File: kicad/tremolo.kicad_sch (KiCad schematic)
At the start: 17 parts, among them IC2 TL072CP

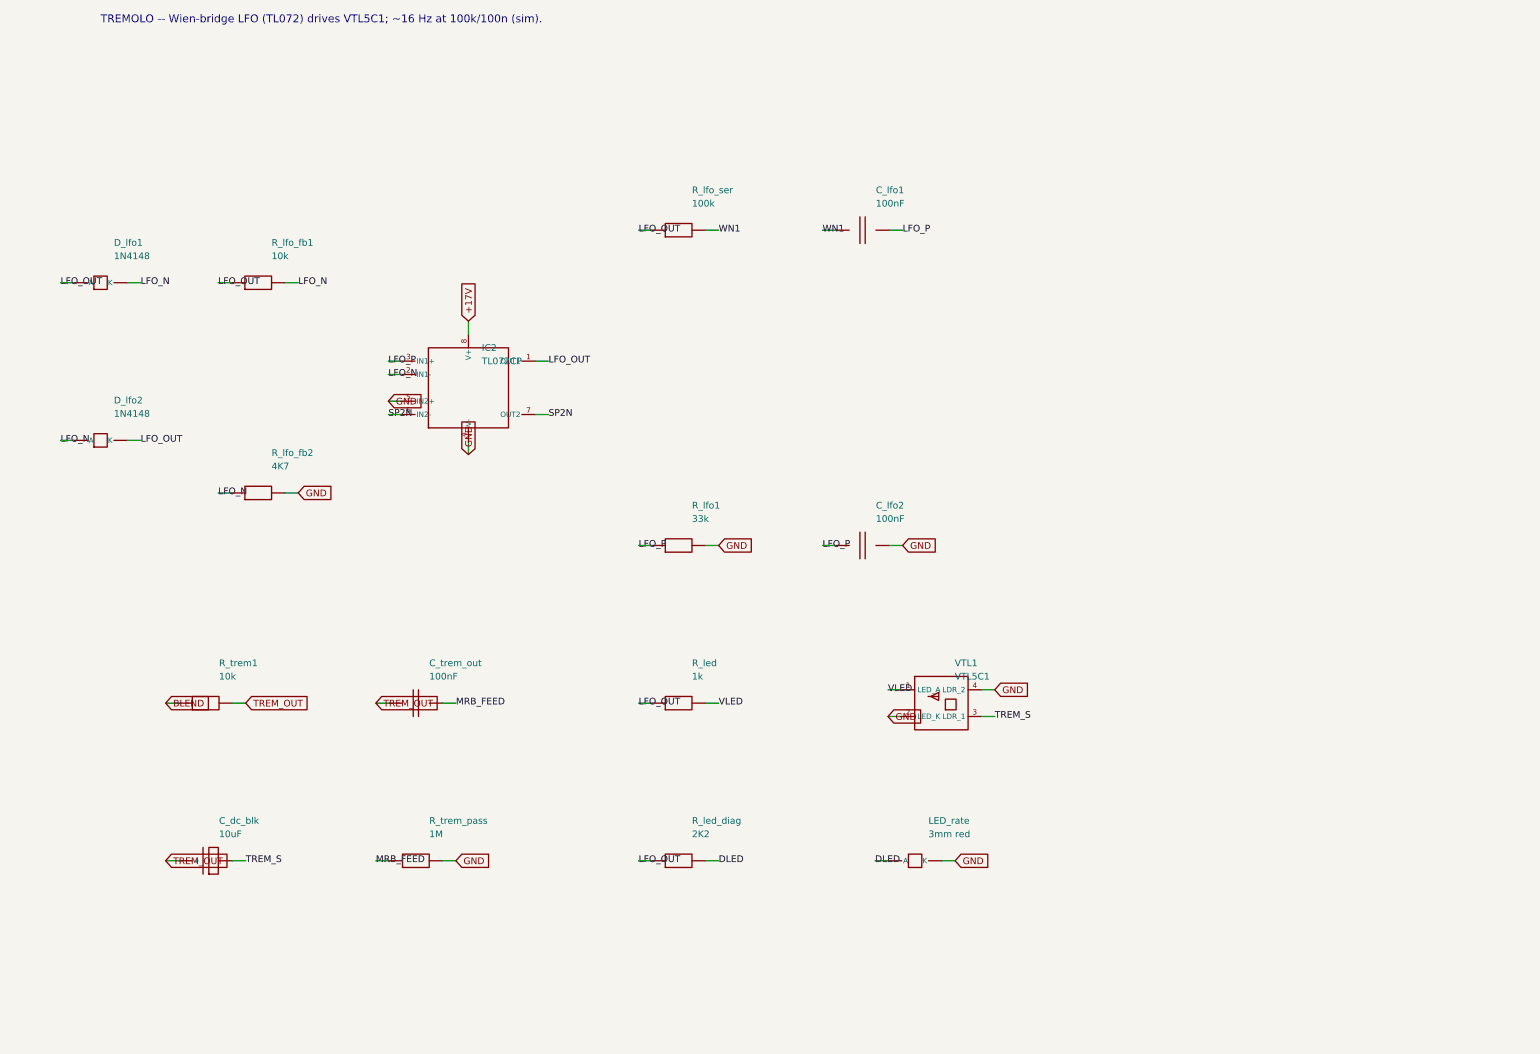
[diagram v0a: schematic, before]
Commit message: Schematic passes KiCad 8 ERC (0 violations); add op-amp mid-rail bias
Installed KiCad 8.0.9 and ran a real Electrical Rules Check on the generated
hierarchy. Drove it to 0 violations:
- snapped every pin/wire endpoint to the 1.27 mm connection grid (was 338
  endpoint_off_grid violations)
- gave the footswitch lines FS_REV/FS_TREM/FS_MRB a real second endpoint via
  100k control pulldowns on the reverb/tremolo/mrb sheets (was 3 dangling labels)

Also made the single-supply TL072 stages electrically real: added a mid-rail
VBIAS network (R_vb1/R_vb2 + C_vb on the Power Supply sheet) and referenced the
reverb driver and tremolo LFO inputs/gain-returns to VBIAS instead of GND
(design addition, flagged in the sheet notes).

Result: kicad-cli 8.0.9 sch erc -> 0 violations; netlist 102 components, 58
nets, 0 unconnected pins; VBIAS spans 10 nodes. Updated SCHEMATIC-BUILD.md,
kicad/README.md, CHANGELOG.md.

https://claude.ai/code/session_01PkrfUi9tvZfLvudJ7h23qD
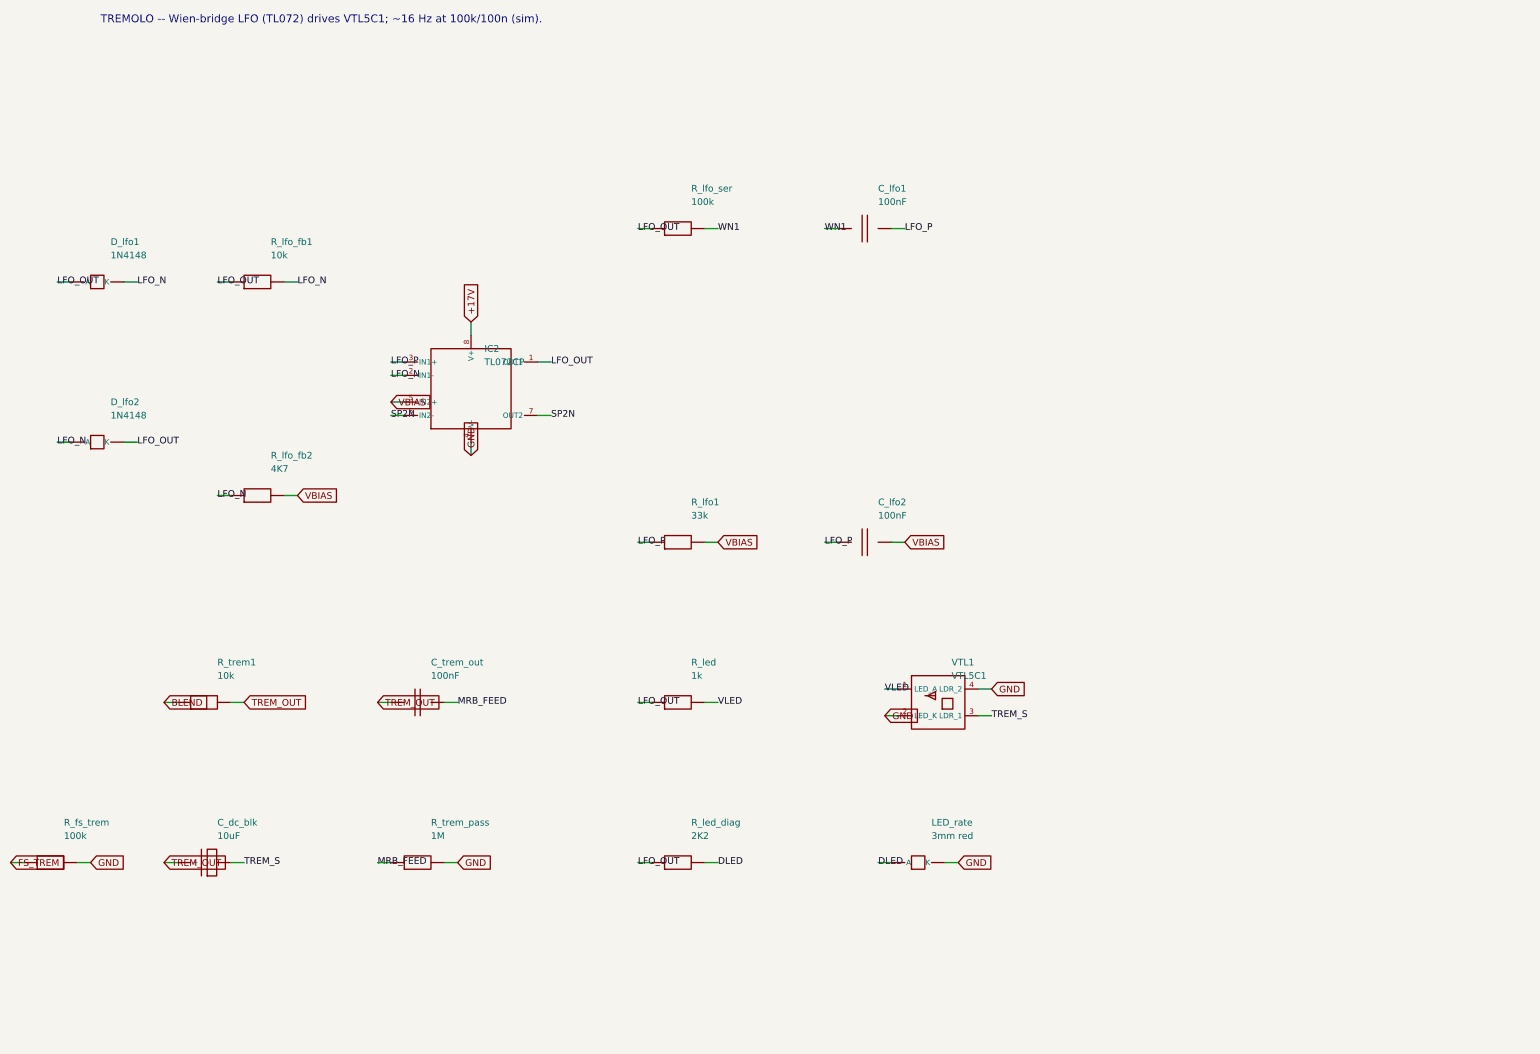
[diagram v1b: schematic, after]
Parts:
- added R_fs_trem: 100k, symbol cr_primitives:R
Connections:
- net GND: now also R_fs_trem.2; no longer C_lfo2.2, IC2.5 (IN2+), R_lfo1.2, R_lfo_fb2.2
- new net FS_TREM: R_fs_trem.1
- new net VBIAS: C_lfo2.2, IC2.5 (IN2+), R_lfo1.2, R_lfo_fb2.2

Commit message: Generate auto-placed PCB (102 footprints, GND pour, board outline)
Build cambridge_reverb.kicad_pcb from the schematic via kicad/gen/gen_pcb.py
(KiCad 8 pcbnew API): assign a THT footprint to every component (standard libs
for generics + the project footprints for VTL5C1 and the 1H toroid), place all
102 footprints (off-board connectors on a bottom wiring-edge strip, toroid in a
reserved spot), assign all 58 nets to pads, draw a 190x115 mm Edge.Cuts outline,
and pour a bottom-layer GND plane. Footprint assignments also carry into the
schematic symbols.

The board opens in KiCad and the ratsnest matches the ERC-clean schematic. It is
placed but NOT routed: kicad-cli pcb drc is dominated by 130 unconnected
(unrouted signal nets; GND is poured) plus cosmetic silk/courtyard overlaps from
dense auto-placement at chassis size -- documented in kicad/PCB-NOTES.md with the
remaining hand-work (placement into floor-plan zones, routing, DRC-to-zero,
Gerbers). Net classes (Default/Power/HighCurrent) carry over for routing.

Also: schematic resistor footprint switched to the compact vertical variant;
gitignore DRC/ERC .rpt reports.

https://claude.ai/code/session_01PkrfUi9tvZfLvudJ7h23qD
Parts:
- C_dc_blk: footprint (none) -> Capacitor_THT:CP_Radial_D8.0mm_P3.50mm
- C_lfo1, C_lfo2, C_trem_out: footprint (none) -> Capacitor_THT:C_Disc_D7.5mm_W2.5mm_P5.00mm
- D_lfo1, D_lfo2: footprint (none) -> Diode_THT:D_DO-41_SOD81_P10.16mm_Horizontal
- IC2: footprint (none) -> Package_DIP:DIP-8_W7.62mm
- LED_rate: footprint (none) -> LED_THT:LED_D3.0mm
- R_fs_trem, R_led, R_led_diag, R_lfo1, R_lfo_fb1, R_lfo_fb2, R_lfo_ser, R_trem1, R_trem_pass: footprint (none) -> Resistor_THT:R_Axial_DIN0207_L6.3mm_D2.5mm_P5.08mm_Vertical
- VTL1: footprint (none) -> cambridge_reverb:VTL5C1

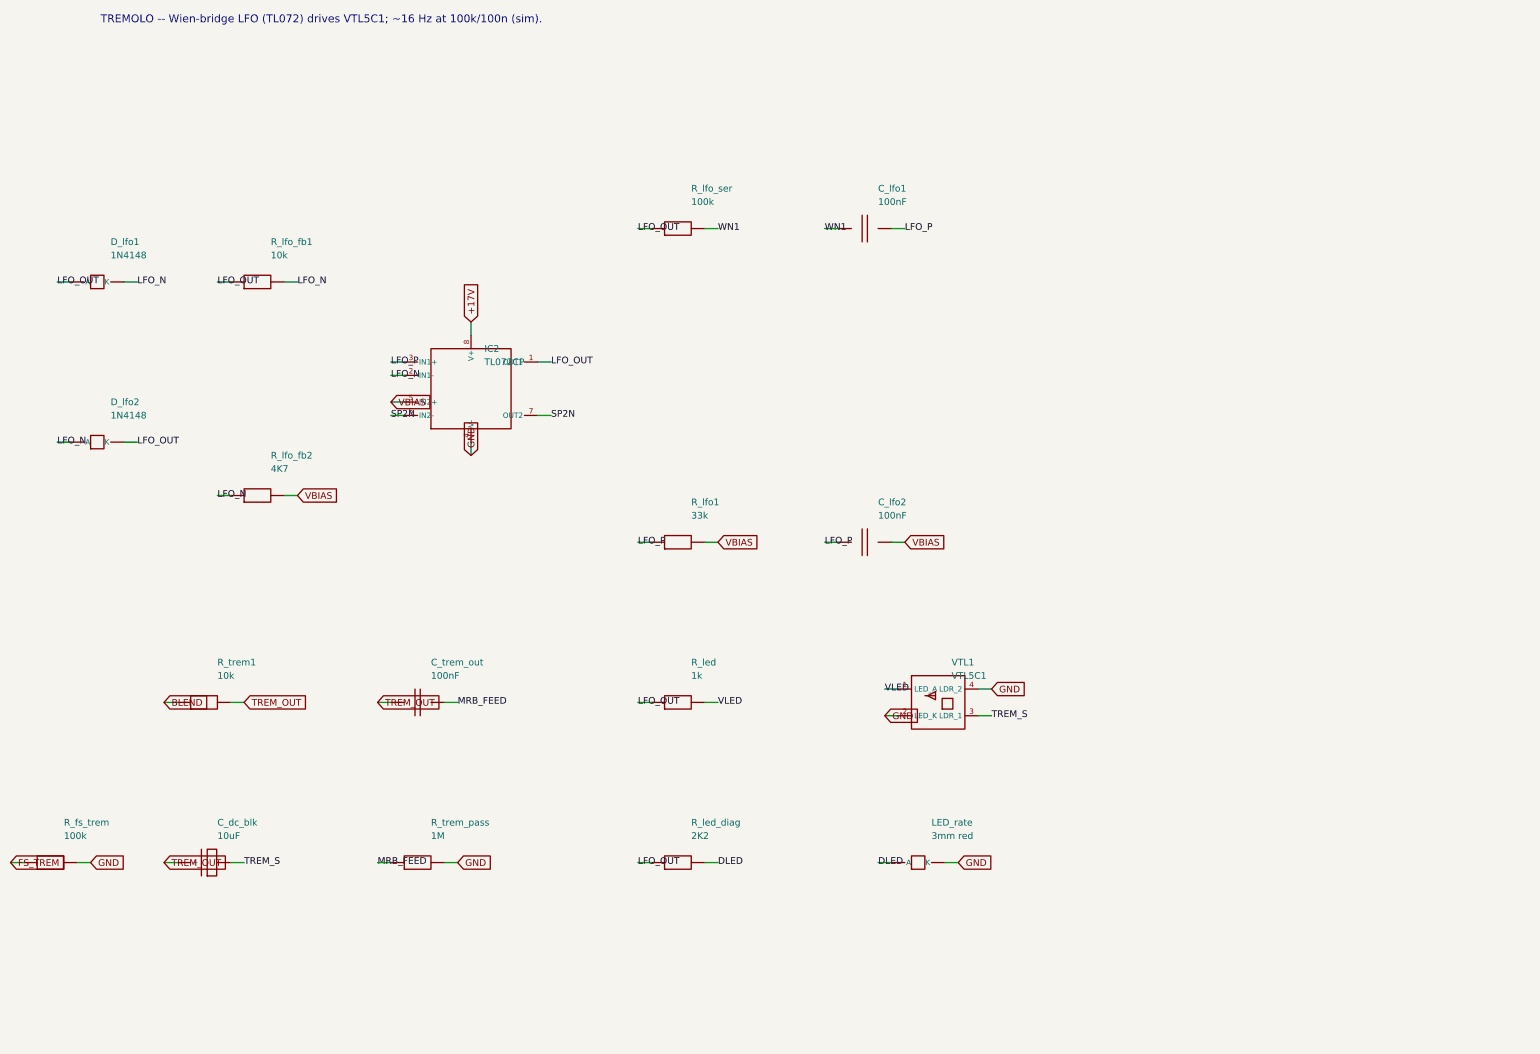
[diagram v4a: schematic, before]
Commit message: Audit pass: center schematic pages, PCB layout audit, SPICE audit
Schematic: gen_kicad.py now defers draw-op emission, computes each sheet's
content bounding box, and translates it to the page center (grid-snapped so pins
stay on the 1.27mm grid). All 8 sheets are centered on the page instead of
crammed top-left; ERC still 0 violations.

PCB: full category-by-category audit in kicad/PCB-AUDIT.md (footprints,
placement, net classes, copper/GND, routing) with prioritized fixes. Applied:
- the 5 reused/off-board pots were modeled with a 16mm panel-pot footprint; they
  are panel-mounted (wired off-board), so they're now 3-pad wiring connectors --
  more correct and a big silk-overlap source removed (packing 51%->48%)
- centered the component grid
Documented findings: LM1875 TO-220-5 annular is 0.0875mm (1.275mm pad on 1.1mm
drill) vs the 0.15mm rule; KBP410G bridge uses a placeholder header footprint;
silk/courtyard overlaps are a density symptom (the 82% packing on the 155x90
safe-bet). Non-routing DRC errors: 9; demo board still 0.

SPICE: audited every netlist/model (spice/README.md). All five run under
ngspice-42 (exit 0) and match the documented numbers; no correctness issues.

https://claude.ai/code/session_01PkrfUi9tvZfLvudJ7h23qD
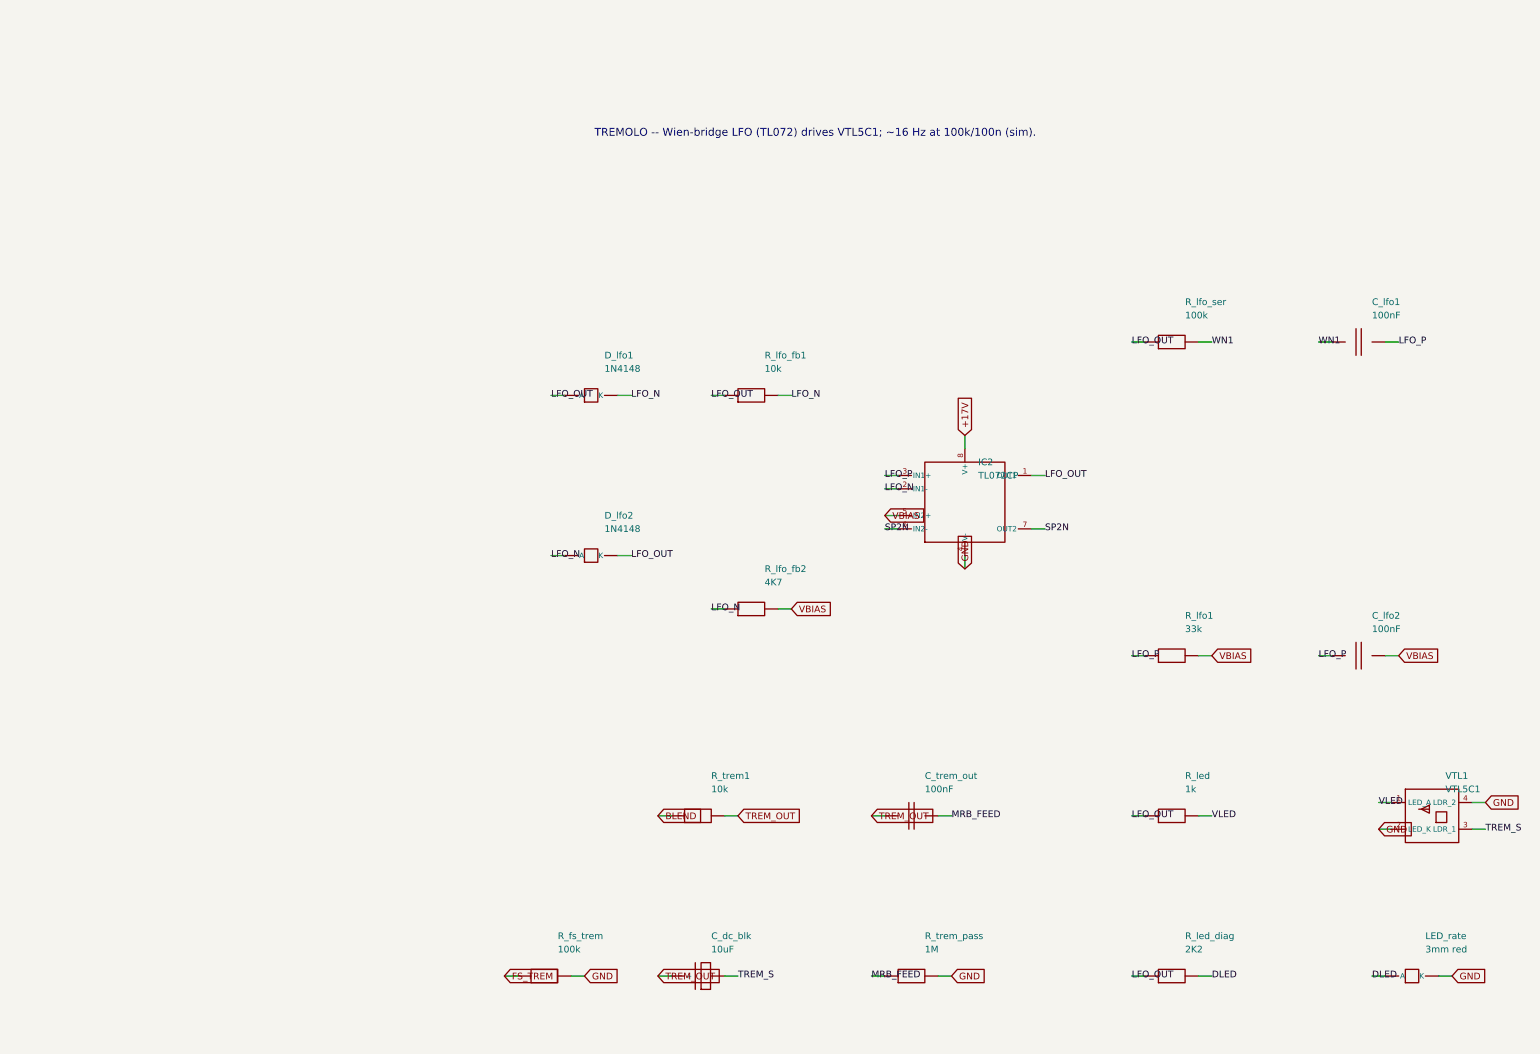
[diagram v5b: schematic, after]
